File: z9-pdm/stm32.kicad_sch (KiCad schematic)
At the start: 57 parts, among them J4 Conn_ST_STDC14, J5 DF40HC3.0-100DS-0.4V51, J7 Conn_TagConnect_2070, SW1 Tactile Button, 160gf, SW2 Tactile Button, 160gf, U3 STM32F427V_G-I_Tx, X1 8MHz 20pF

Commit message: x
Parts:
- removed TP22, TP23, TP28, TP31, TP32, TP33, TP34, TP35, TP36, TP37, TP38: PE0, TestPoint:TestPoint_Pad_D1.0mm, symbol dnt_global:TestPoint_Pad_D1.0mm
- J5: now fitted; now in the parts list
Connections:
- net BOOT1: no longer J5.20
- net PA10: now also J5.34
- net PA8: now also J5.81
- net PB10: now also J5.60; no longer J5.32
- net PB11: now also J5.59; no longer J5.33
- net PB12: now also J5.61; no longer J5.34
- net PB8: no longer U3.95 (PB8)
- net PB9: no longer U3.96 (PB9)
- net PC13: no longer J5.40
- net PC14: no longer J5.41
- net PC15: now also J5.40; no longer J5.42
- net PC7: now also J5.77; no longer J5.37
- net PC8: now also J5.78; no longer J5.38
- net PC9: no longer J5.39
- net PD10: now also J5.69; no longer J5.44
- net PD11: now also J5.70; no longer J5.43
- net PD12: now also J5.71
- net PD13: now also J5.72
- net PD14: now also J5.73
- net PD15: now also J5.74
- net PD7: no longer U3.88 (PD7)
- net PD8: now also J5.66; no longer J5.46
- net PD9: now also J5.67; no longer J5.45
- net PE0: no longer U3.97 (PE0)
- net PE1: no longer U3.98 (PE1)
- net PE12: now also J5.36; no longer J5.49
- net PE7: now also J5.42
- net PE8: now also J5.41
- net SPI2_CS: now also J5.79
- net SPI2_IRQ: now also J5.63
- net SPI2_IRQ2: now also J5.64
- net SPI2_SCK: now also J5.62
- net SPI2_SDI: now also J5.80
- net SPI2_SDO: now also J5.83
- net VIPOWER_PWM: now reaches J5.75
- new net ESP_BOOT: U3.96 (PB9)
- new net ESP_EN: U3.95 (PB8)
- new net UART8_RX: U3.97 (PE0)
- new net UART8_TX: U3.98 (PE1)
- no-connect marks 77 -> 63

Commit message: pre kc update
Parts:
- removed TP19, TP20, TP21, TP24, TP25, TP26, TP3, TP6: PE0, TestPoint:TestPoint_Pad_D1.0mm, symbol dnt_global:TestPoint_Pad_D1.0mm
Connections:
- net LCD_LED is gone; now on net PD4: U3.85 (PD4)
- net LCD_ON is gone; now on net PE14: U3.45 (PE14)
- net LCD_RESET is gone; now on net PD3: U3.84 (PD3)
- net PB9 is gone; now on net PC15: J5.31
- net VIPOWER_PWM is gone; now on net TIM3_CH1: J5.75
- net +3.3V: now also J5.1, J5.2, J5.3, J5.4, J5.5, J5.6; no longer J5.26
- net ESP_EN: now also J5.43
- net GND: now also J5.51, J5.52, J5.53, J5.54, J5.55, J5.56; no longer J5.28
- net PA8: now also J5.82; no longer J5.19, J5.81
- net PB1: now also J5.26
- net PB10: now also J5.59; no longer J5.60
- net PB11: now also J5.58; no longer J5.59
- net PB4: now also J5.46; no longer J5.22
- net PB5: now also J5.47; no longer J5.21
- net PC13: now also J5.35
- net PC15: no longer J5.40
- net PC9: now also J5.81
- net PD7: now also J5.48, U3.88 (PD7); no longer J5.47
- net PE10: now also J5.39; no longer J5.10
- net PE11: now also J5.38; no longer J5.50
- net PE7: no longer J5.13
- net PE8: no longer J5.12
- net PE9: now also J5.40; no longer J5.11
- net SPI4_CS_1: now also J5.94
- net SPI4_CS_2: now also J5.96
- net SPI4_IRQ: now also J5.93
- net SPI4_SCK: now also J5.95
- net SPI4_SDI: now also J5.92
- net SPI4_SDO: now also J5.91
- net SYS_WKUP: now also J5.28
- net USART2_RX: now reaches J5.100
- net USART2_RX: now also U3.87 (PD6)
- net PD3: now reaches J5.97
- net PD4: now reaches J5.98
- net USART2_TX: now reaches J5.99
- net USART2_TX: now also U3.86 (PD5)
- net PE14: now reaches J5.24
- net PA5: now reaches J5.27
- net PA5: now also U3.30 (PA5)
- net +5V: now reaches J5.44
- net +5V: now also J5.45
- net PA4: no longer names the net of J5.18
- net PB8: no longer names the net of J5.25
- net PE0: no longer names the net of J5.15
- net PE1: no longer names the net of J5.14
- net SENSOR_ON renamed PE15
- net PE15: now also J5.60
- no-connect marks 63 -> 40
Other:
- moved on the sheet: J5A

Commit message: new fuse and ideal diode
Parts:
- C11: renamed from C16; footprint PCM_JLCPCB:C_0402 -> dnt:C_0402_1005Metric
- C12: renamed from C15; footprint PCM_JLCPCB:C_0402 -> dnt:C_0402_1005Metric
- C13: renamed from C12; footprint PCM_JLCPCB:C_0402 -> dnt:C_0402_1005Metric
- C15: renamed from C11; footprint PCM_JLCPCB:C_0402 -> dnt:C_0402_1005Metric
- C16: renamed from C30; footprint PCM_JLCPCB:C_0402 -> dnt:C_0402_1005Metric
- C22: renamed from C26; footprint PCM_JLCPCB:C_0603 -> dnt:C_0603_1608Metric; symbol PCM_JLCPCB-Capacitors:0603,10uF,(2) -> dnt_global:0603,10uF,_25V
- C26: renamed from C9; footprint PCM_JLCPCB:C_0603 -> dnt:C_0603_1608Metric; symbol PCM_JLCPCB-Capacitors:0603,100nF -> dnt_global:0603 100nF 50V X7R
- C8: renamed from C706; footprint PCM_JLCPCB:C_0402 -> dnt:C_0402_1005Metric
- C9: renamed from C17; footprint PCM_JLCPCB:C_0402 -> dnt:C_0402_1005Metric
- J4: renamed from J5; value DF40HC3.0-100DS-0.4V51 -> DF40HC(3.0)-100DS-0.4V(51)
- renumbered C20 to C14, C13 to C17, C14 to C20, C1 to C23, C23 to C24, C8 to C25, D4 to D11, D5 to D13, D6 to D14, D11 to D15, D7 to D4, D14 to D5, D15 to D6, D16 to D7, FB1 to FB2, J4 to J2, J7 to J3, R45 to R12, R36 to R19, R35 to R20, R6 to R21, R43 to R6, RN1 to RN2, RN2 to RN3, SW1 to SW2, SW2 to SW3, X1 to X2
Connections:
- net PB10 renamed TIM2_CH3
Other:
- moved on the sheet: C11, C12, C13, C15, C16, C22, C8, C9

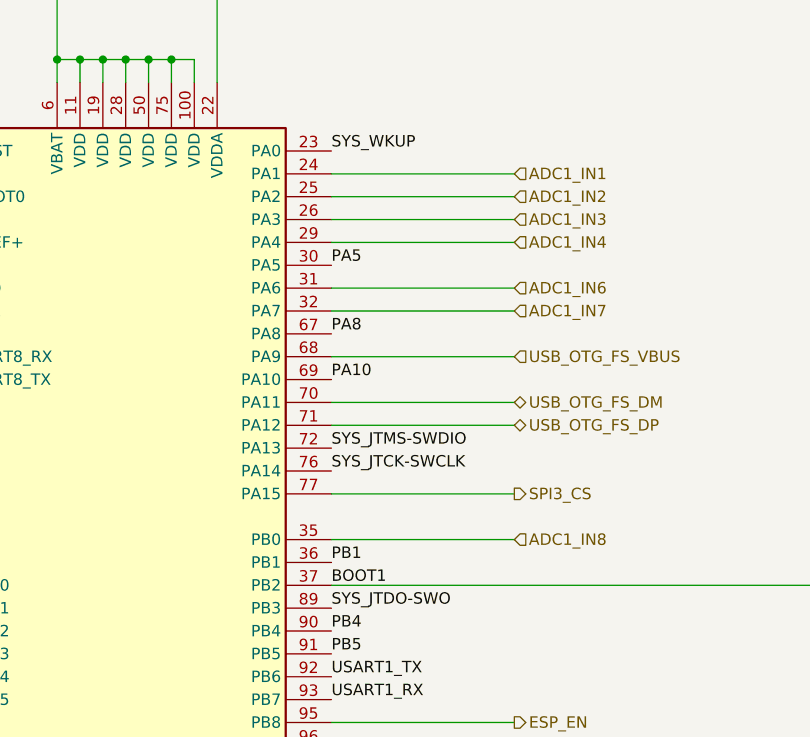
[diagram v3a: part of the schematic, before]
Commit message: post 5v lay references lost
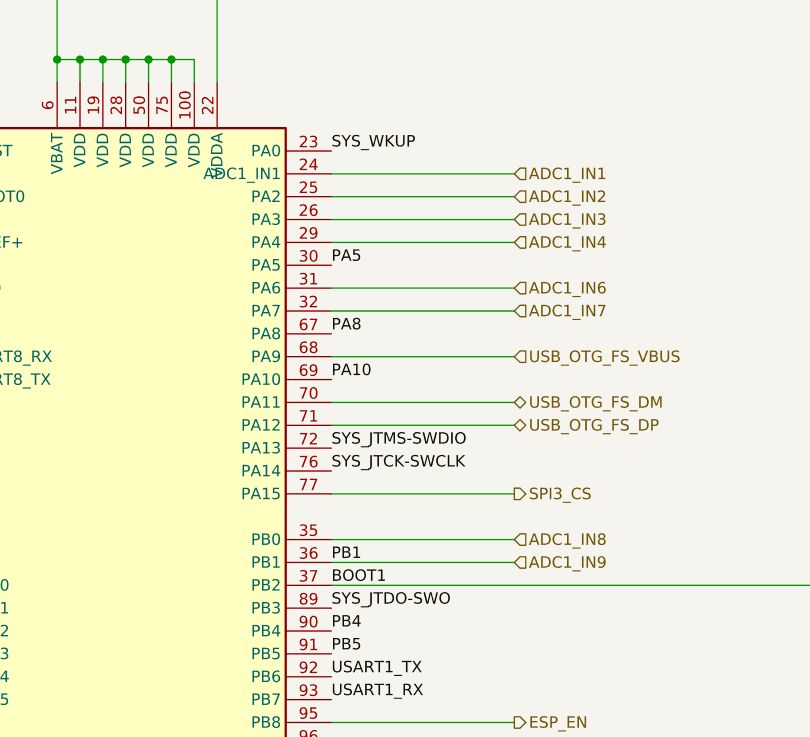
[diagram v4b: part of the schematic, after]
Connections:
- net PB1 renamed ADC1_IN9

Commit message: pre final pdm erc
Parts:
- removed D4, D7: LED-YELLOW, dnt:LED_0603_1608Metric - polarity, symbol dnt_global:LED-YELLOW
- removed D5: LED-WHITE, dnt:LED_0603_1608Metric - polarity, symbol dnt_global:LED-WHITE
- removed D6: LED-RED, dnt:LED_0603_1608Metric - polarity, symbol dnt_global:LED-RED
- removed RN2: 1k, Resistor_SMD:R_Array_Convex_4x0603, symbol dnt_global:R_Pack04_-_1K

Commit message: x
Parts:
- J2: footprint dnt:Conn_SAMTEC_FTSH-107-01-F-DV-K-Fix -> dnt:SAMTEC_FTSH-107-01-F-DV-K-Fix; LCSC (none) -> C5563894
- J4: LCSC (none) -> C424649
- RN2: renamed from RN3; Part # (none) -> CAT16-1001F4LF
- renumbered C8 to C11, C9 to C12, C11 to C13, C12 to C14, C14 to C15, C13 to C16, C15 to C17, C16 to C18, C17 to C19, C22 to C21, C23 to C22, C24 to C23, C25 to C24, C26 to C25, D11 to D3, D13 to D4, D14 to D5, D15 to D6, R6 to R12, R12 to R13, R19 to R14, R20 to R15, R21 to R16, U3 to U6

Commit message: passes sch drc
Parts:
- J2: footprint dnt:SAMTEC_FTSH-107-01-F-DV-K-Fix -> dnt:Conn_SAMTEC_FTSH-107-01-F-DV-K-Fix

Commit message: jlc
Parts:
- J2: now left out of the parts list
